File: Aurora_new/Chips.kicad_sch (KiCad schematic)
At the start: 87 parts, among them J1 UJ20-C-H-C-3-SMT-TR, J16 PPPC042LFBN-RC, J3 PPPC042LFBN-RC, J36 PPPC042LFBN-RC, J41 STEMMA QT, J50 PCB.RPSMAFRA.HT, J6 DM3AT-SF-PEJM5, U1 STM32H757BITx, U13 XBP9X-DMUS-001, U14 MS5611-01BA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

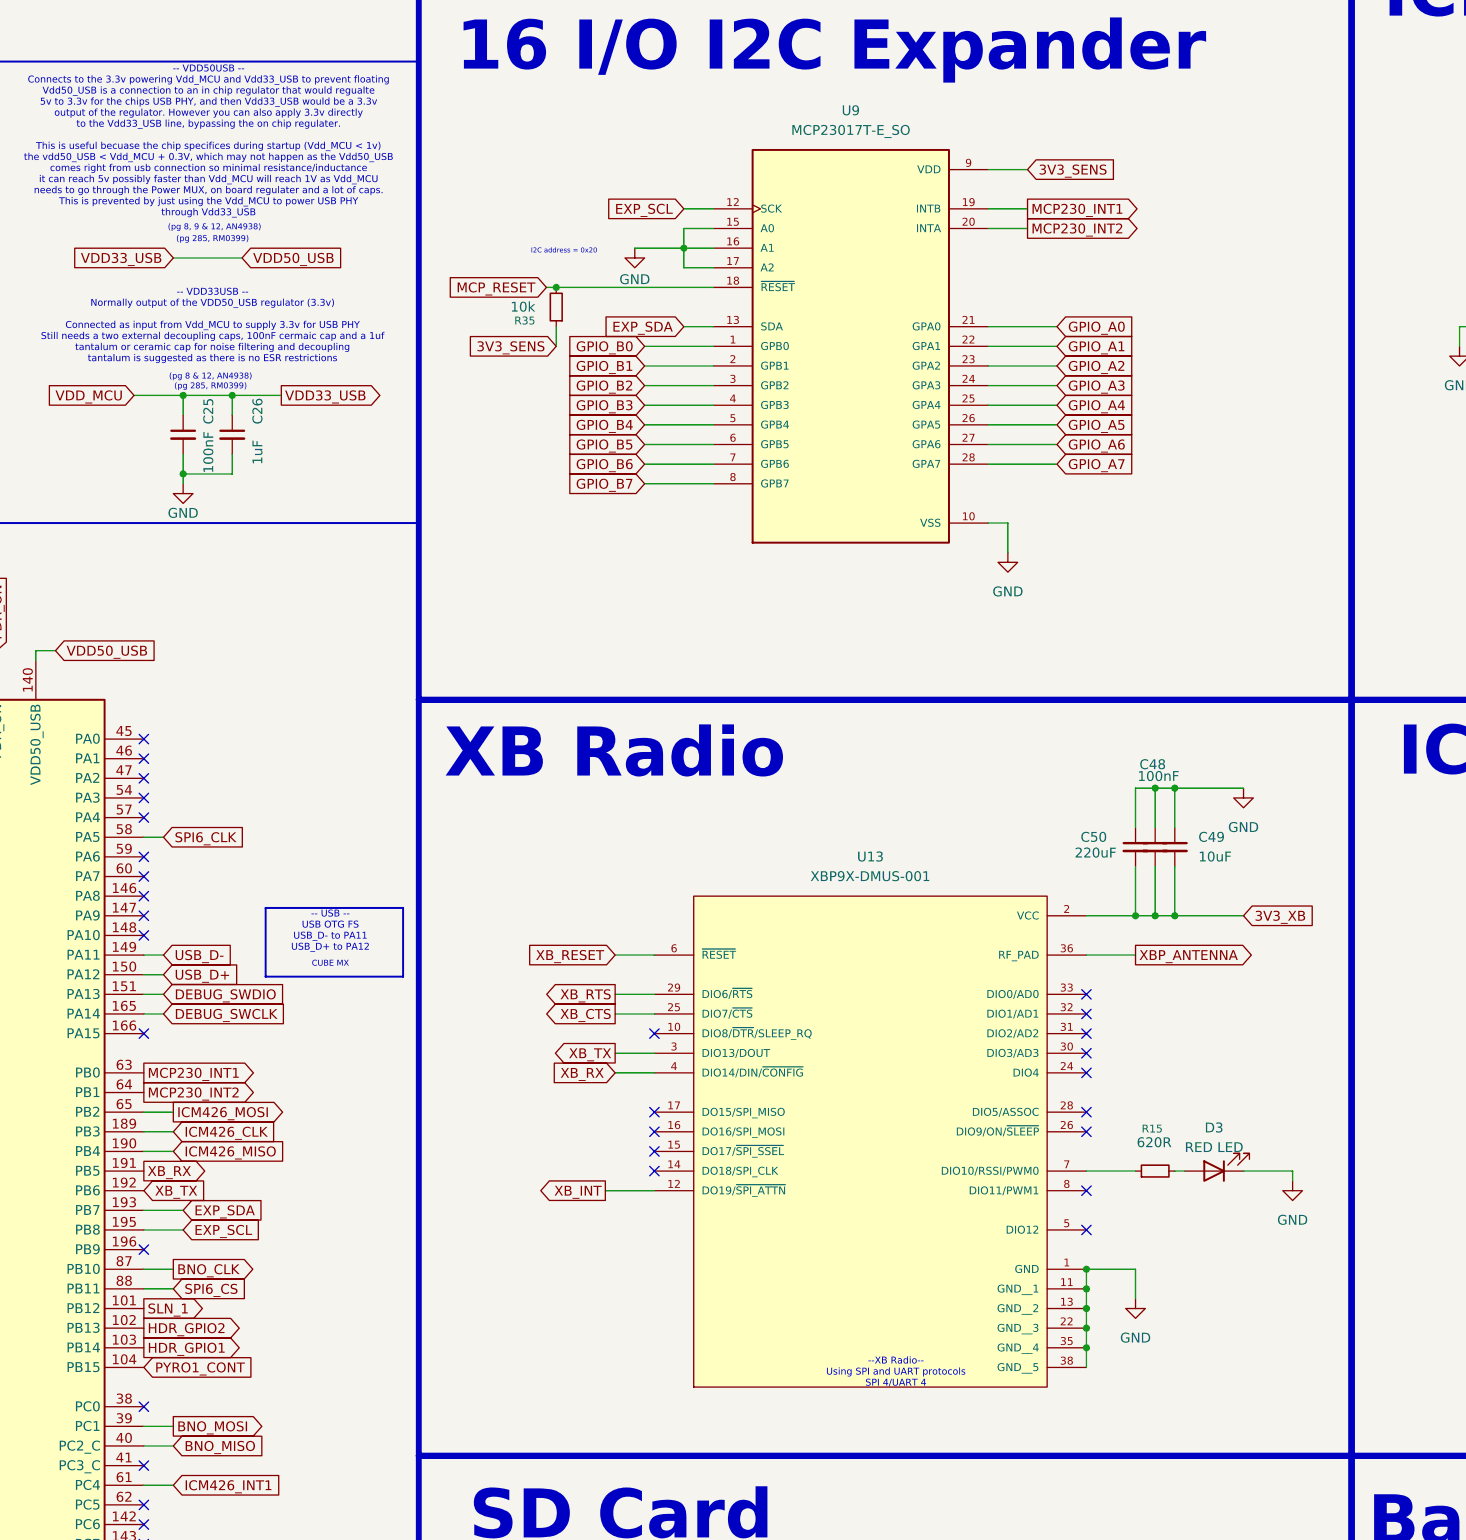
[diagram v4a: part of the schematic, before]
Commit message: fixed schematic issues, started organizing components in PCB
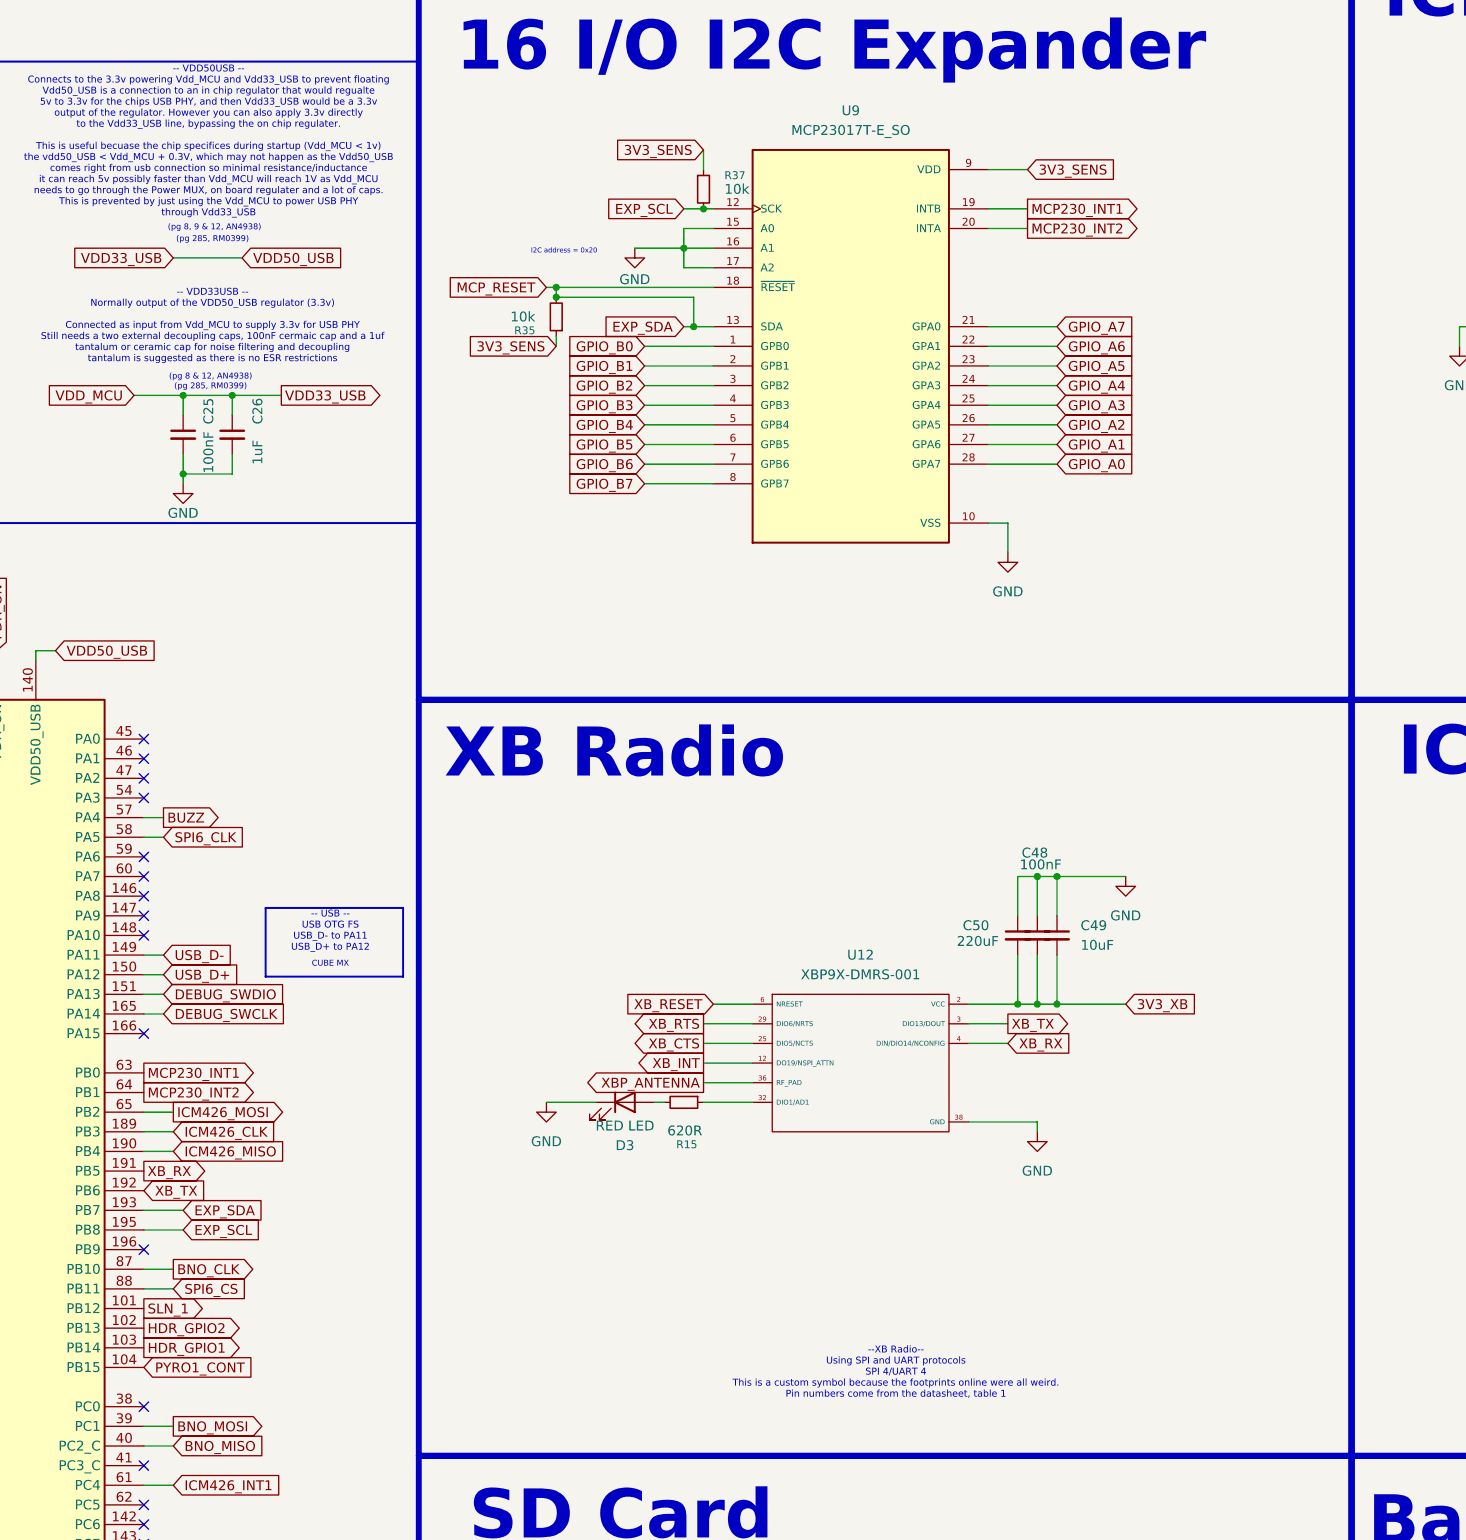
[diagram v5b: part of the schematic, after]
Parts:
- removed U13: XBP9X-DMUS-001, XBP9X-DMUS-001:XCVR_XBP9X-DMUS-001, symbol XBP9X-DMUS-001:XBP9X-DMUS-001
- added R37: 10k, Resistor_SMD:R_0805_2012Metric, symbol Device:R_Small
- added U12: XBP9X-DMRS-001, XBP9X_DMUS_021:XCVR_XBP9X-DMUS-021, symbol XBP9X-DMUS-021:XB_SYM
- U6: footprint ICM-42688-P:PQFN50P300X250X97-14N -> ICM_42688_P:PQFN50P300X250X97-14N
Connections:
- net MCP_RESET is gone; now on net EXP_SDA: R35.2, U1.66 (PI15), U9.18 (~{RESET})
- net 3V3_SENS: now also R37.1
- net 3V3_XB: now also U12.2 (VCC)
- net EXP_SCL: now also R37.2
- net GND: now also U12.38 (GND)
- net GPIO_A0: now also U9.28 (GPA7); no longer U9.21 (GPA0)
- net GPIO_A1: now also U9.27 (GPA6); no longer U9.22 (GPA1)
- net GPIO_A2: now also U9.26 (GPA5); no longer U9.23 (GPA2)
- net GPIO_A3: now also U9.25 (GPA4); no longer U9.24 (GPA3)
- net GPIO_A4: now also U9.24 (GPA3); no longer U9.25 (GPA4)
- net GPIO_A5: now also U9.23 (GPA2); no longer U9.26 (GPA5)
- net GPIO_A6: now also U9.22 (GPA1); no longer U9.27 (GPA6)
- net GPIO_A7: now also U9.21 (GPA0); no longer U9.28 (GPA7)
- net XBP_ANTENNA: now also U12.36 (RF_PAD)
- net XB_CTS: now also U12.25 (DIO5/NCTS)
- net XB_INT: now also U12.12 (DO19/NSPI_ATTN)
- net XB_RESET: now also U12.6 (NRESET)
- net XB_RTS: now also U12.29 (DIO6/NRTS)
- net XB_RX: now also U12.4 (DIN/DIO14/NCONFIG)
- net XB_TX: now also U12.3 (DIO13/DOUT)
- net BUZZ: now reaches U1.57 (PA4)
- net at R15.1: now also U12.32 (DIO1/AD1)
- no-connect marks 85 -> 70
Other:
- note added: "--XB Radio-- Using SPI and UART protocols SPI 4/UART 4 This is a custom symbol because the footprints online were all weird. Pin numbers come from the datasheet, table 1"
- note removed: "--XB Radio-- Using SPI and UART protocols SPI 4/UART 4"
- moved on the sheet: C48, C49, C50, D3, R15, R35
